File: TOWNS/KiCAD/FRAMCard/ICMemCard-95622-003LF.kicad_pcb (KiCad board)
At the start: 2 copper layers, 79.1 x 50.5 mm, 19 parts, among them J1 PCMCIA_Connector, Q1 BC846X, Q2 BC846X, U1 FM18W08-SGTR, U2 FM18W08-SGTR, U3 74AHCT1G32

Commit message: MOving files around.
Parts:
- U3: value 74AHCT1G32 -> SN74LS32DR; footprint PCMCIA:SOT353_Easy -> Package_SO:SOIC-14_3.9x8.7mm_P1.27mm
- moved R6 30.0 mm to (106.9, 77.0), turned to 180 degrees
- moved R5 20.3 mm to (95.9, 87.9)
- moved U3 14.6 mm to (84.5, 81.8), turned to 270 degrees
- moved C1 3.56 mm to (80.4, 93.5)
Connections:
- R1 pad 2: /~OE -> Net-(R1-Pad2)
- R3 pad 2: /~WE~orWP -> Net-(R3-Pad2)
- U3 pad 1: /Wp -> /WPorWP
- U3 pad 3: GND -> /~WE~orWP
- U3 pad 4: /~WE~orWP -> /Wp
- U3 pad 5: Vcc -> /Wp
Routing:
- net /~WE~orWP: track 130.8 -> 80.5 mm, vias 4 -> 3
- net Net-(R3-Pad2): track 0.00 -> 35.3 mm, vias 0 -> 2
- net /~CE2: track 71.0 -> 43.6 mm, vias 3 -> 1
- net GND: track 555.9 -> 529.5 mm
- net Net-(R1-Pad2): track 0.00 -> 22.5 mm, vias 0 -> 2
- net /~CE1: track 92.8 -> 70.8 mm, vias 4 -> 2
- net /WPorWP: track 0.00 -> 12.5 mm
- net Vcc: track 282.4 -> 293.6 mm, vias 4 -> 7
- net /Wp: track 96.8 -> 106.9 mm
- net /~OE: track 132.8 -> 123.2 mm
- net /~WE: track 73.6 -> 64.2 mm
- net Net-(D2-Pad1): track 29.3 -> 28.0 mm
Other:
- board text added: "FM TOWNS RESCUE BOOT MEMORY CARD by Captain YS http://www.ysflight.com Ver. 20220520"
- board text removed: "FM TOWNS RESCUE BOOT MEMORY CARD by Captain YS http://www.ysflight.com Ver. 20220514"

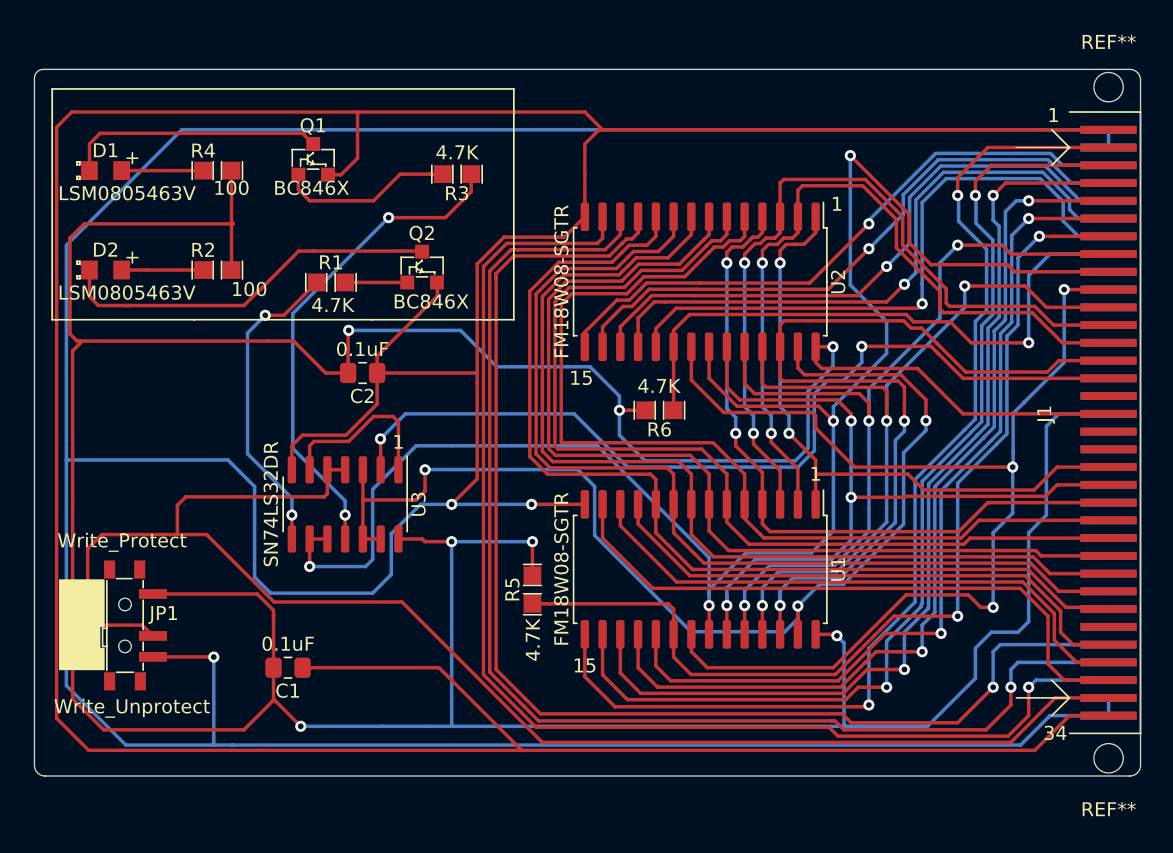
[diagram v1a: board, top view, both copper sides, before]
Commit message: Moving files around.
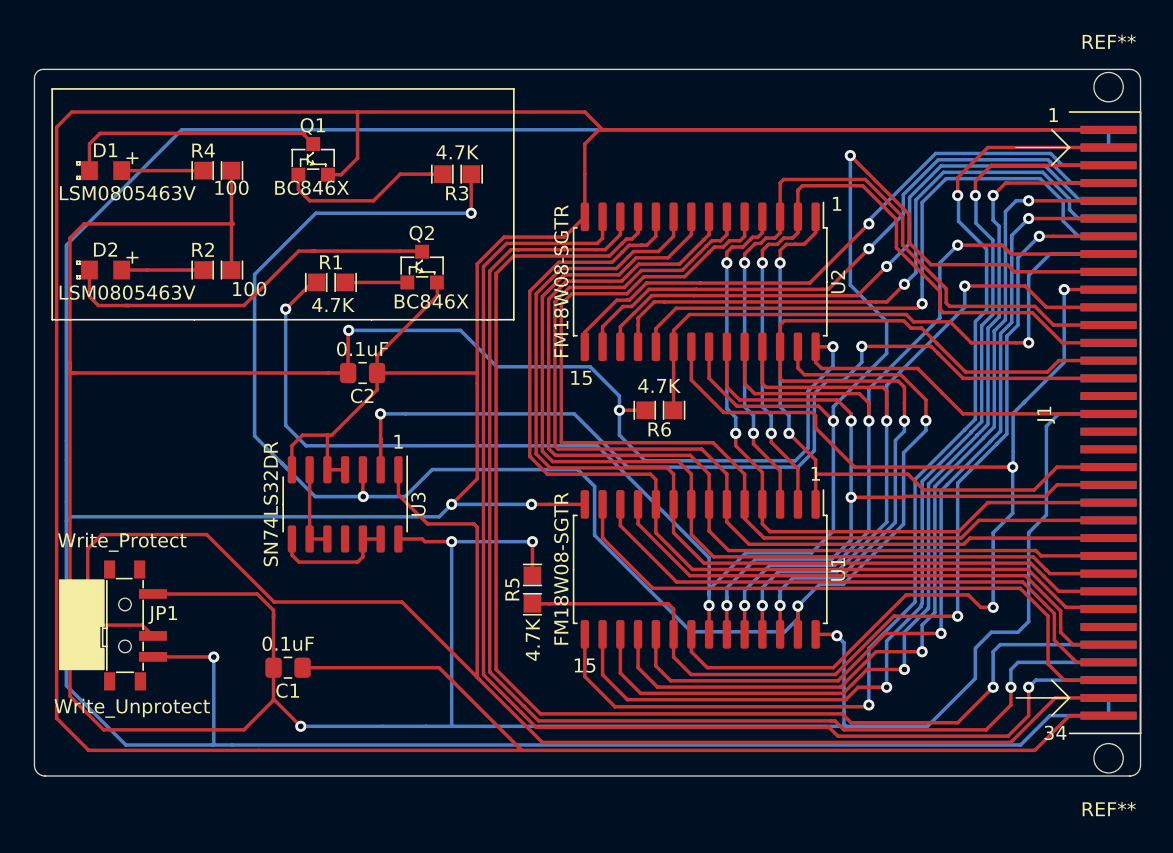
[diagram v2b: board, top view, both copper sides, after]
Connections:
- J1 pad 33: /Wp -> /WP
- JP1 pad 2: /Wp -> /WP
- R1 pad 2: Net-(R1-Pad2) -> /~OE
- R3 pad 2: Net-(R3-Pad2) -> /~WE~orWP
- U3 pad 1: /WPorWP -> /WP
- U3 pad 10: /~OE -> Net-(U3-Pad10)
- U3 pad 11: Net-(R3-Pad2) -> Net-(U3-Pad11)
- U3 pad 12: /~WE~orWP -> Net-(U3-Pad12)
- U3 pad 13: /~WE~orWP -> Net-(U3-Pad12)
- U3 pad 4: /Wp -> GND
- U3 pad 5: /Wp -> GND
- U3 pad 6: /WPorWP -> Net-(U3-Pad10)
- U3 pad 8: Net-(R1-Pad2) -> Net-(U3-Pad12)
- U3 pad 9: /~OE -> Net-(U3-Pad10)
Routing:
- net /WP: track 0.00 -> 110.1 mm
- net /Wp: track 106.9 -> 0.00 mm
- net /~WE~orWP: track 80.5 -> 117.1 mm, vias 3 -> 4
- net Net-(R3-Pad2): track 35.3 -> 0.00 mm, vias 2 -> 0
- net Net-(R1-Pad2): track 22.5 -> 0.00 mm, vias 2 -> 0
- net /WPorWP: track 12.5 -> 0.00 mm
- net Net-(U3-Pad12): track 0.00 -> 9.13 mm
- net GND: track 529.5 -> 521.1 mm
- net Net-(U3-Pad10): track 0.00 -> 6.22 mm
- net /~OE: track 123.2 -> 127.1 mm
- net /~WE: track 64.2 -> 65.7 mm

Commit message: Updated version number
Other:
- board text added: "FM TOWNS RESCUE BOOT MEMORY CARD by Captain YS http://www.ysflight.com Ver. 20220525"
- board text removed: "FM TOWNS RESCUE BOOT MEMORY CARD by Captain YS http://www.ysflight.com Ver. 20220520"
